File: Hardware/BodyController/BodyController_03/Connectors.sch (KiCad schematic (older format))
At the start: 10 parts, among them J1 7807, J10 7807, J11 7807, J2 CONN_01X08, J3 CONN_01X06, J5 CONN_01X14, J6 CONN_01X02, J7 CONN_01X06, J8 USB_OTG, J9 CONN_01X14

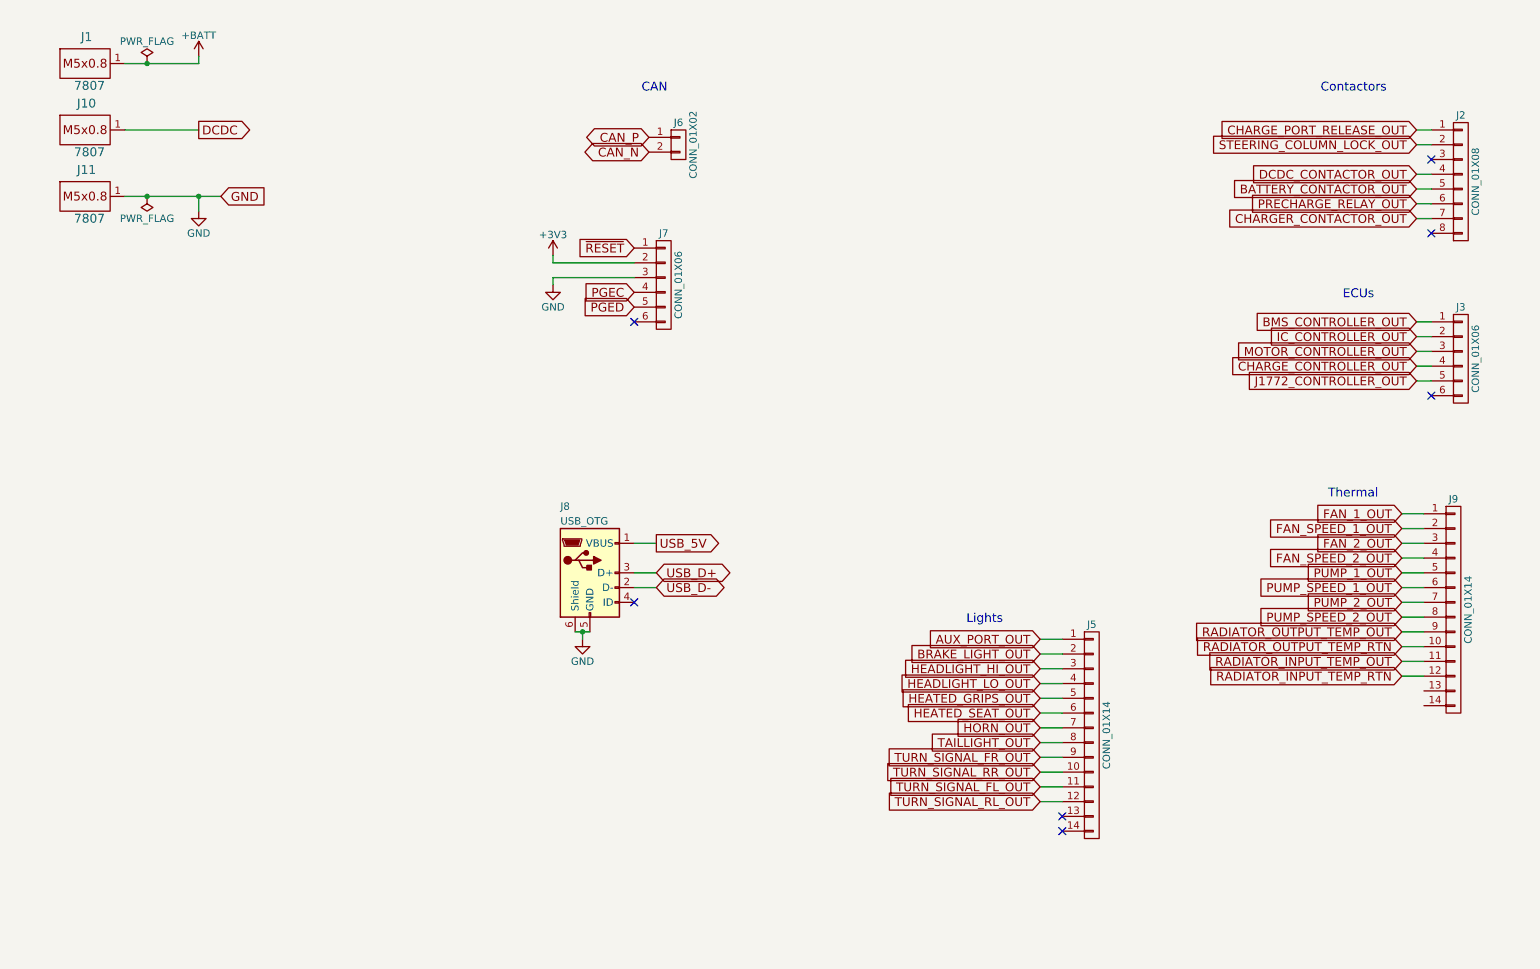
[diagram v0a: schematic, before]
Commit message: Updated layout, cleaned up directory, and modified BOM
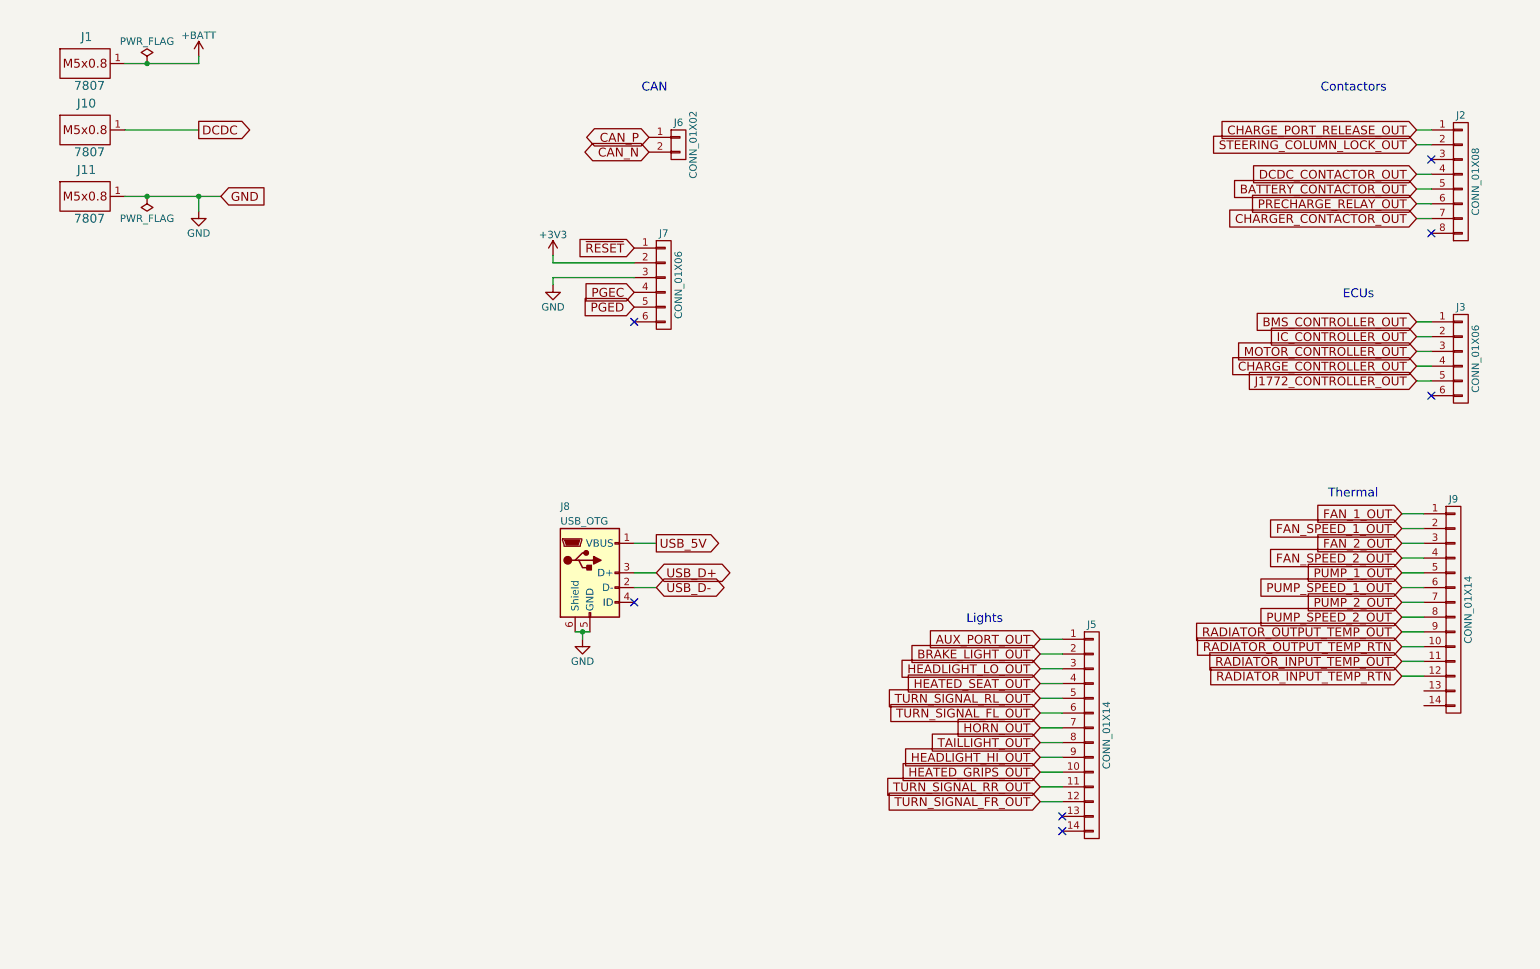
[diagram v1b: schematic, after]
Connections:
- net HEADLIGHT_HI_OUT: now also J5.9 (P9); no longer J5.3 (P3)
- net HEADLIGHT_LO_OUT: now also J5.3 (P3); no longer J5.4 (P4)
- net HEATED_GRIPS_OUT: now also J5.10 (P10); no longer J5.5 (P5)
- net HEATED_SEAT_OUT: now also J5.4 (P4); no longer J5.6 (P6)
- net TURN_SIGNAL_FL_OUT: now also J5.6 (P6); no longer J5.11 (P11)
- net TURN_SIGNAL_FR_OUT: now also J5.12 (P12); no longer J5.9 (P9)
- net TURN_SIGNAL_RL_OUT: now also J5.5 (P5); no longer J5.12 (P12)
- net TURN_SIGNAL_RR_OUT: now also J5.11 (P11); no longer J5.10 (P10)
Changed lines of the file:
@@
 EESchema Schematic File Version 2
+LIBS:BodyController_03-rescue
 LIBS:power
 LIBS:device
@@
 LIBS:contrib
 LIBS:valves
-LIBS:HSD
-LIBS:micros
-LIBS:ICs
-LIBS:Connectors
 LIBS:BodyController_03-cache
 EELAYER 25 0
@@
 Text GLabel 7500 4950 0    59   Input ~ 0
 AUX_PORT_OUT
+Text GLabel 7500 5750 0    59   Input ~ 0
+HEADLIGHT_HI_OUT
 Text GLabel 7500 5150 0    59   Input ~ 0
-HEADLIGHT_HI_OUT
+HEADLIGHT_LO_OUT
+Text GLabel 7500 6050 0    59   Input ~ 0
+TURN_SIGNAL_FR_OUT
+Text GLabel 7500 5950 0    59   Input ~ 0
+TURN_SIGNAL_RR_OUT
+Text GLabel 7500 5450 0    59   Input ~ 0
+TURN_SIGNAL_FL_OUT
+Text GLabel 7500 5350 0    59   Input ~ 0
+TURN_SIGNAL_RL_OUT
+Text GLabel 7500 5850 0    59   Input ~ 0
+HEATED_GRIPS_OUT
 Text GLabel 7500 5250 0    59   Input ~ 0
-HEADLIGHT_LO_OUT
-Text GLabel 7500 5750 0    59   Input ~ 0
-TURN_SIGNAL_FR_OUT
-Text GLabel 7500 5850 0    59   Input ~ 0
-TURN_SIGNAL_RR_OUT
-Text GLabel 7500 5950 0    59   Input ~ 0
-TURN_SIGNAL_FL_OUT
-Text GLabel 7500 6050 0    59   Input ~ 0
-TURN_SIGNAL_RL_OUT
-Text GLabel 7500 5350 0    59   Input ~ 0
-HEATED_GRIPS_OUT
-Text GLabel 7500 5450 0    59   Input ~ 0
 HEATED_SEAT_OUT
 Text GLabel 7500 5650 0    59   Input ~ 0
@@
 	1800 1950 1800 2050
 Wire Wire Line
-	1300 1950 1450 1950
-Wire Wire Line
-	1450 1950 1800 1950
-Wire Wire Line
-	1800 1950 1950 1950
+	1300 1950 1950 1950
 Wire Wire Line
 	1800 1050 1800 1000
 Wire Wire Line
-	1300 1050 1450 1050
-Wire Wire Line
-	1450 1050 1800 1050
+	1300 1050 1800 1050
 Wire Wire Line
 	1800 1500 1300 1500
@@
 	4900 4600 4750 4600
 Wire Wire Line
-	4350 4900 4400 4900
-Wire Wire Line
-	4400 4900 4450 4900
+	4350 4900 4450 4900
 Wire Wire Line
 	4400 4950 4400 4900

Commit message: started serious layout
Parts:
- removed J1, J10, J11: 7807, Footprints:7807, symbol 7807
- removed J2: CONN_01X08, Connectors_Molex:Molex_MegaFit_2x04x5.70mm_Straight, symbol CONN_01X08
- removed J3: CONN_01X06, Connectors_Molex:Molex_MegaFit_2x03x5.70mm_Straight, symbol CONN_01X06
- removed J5, J9: CONN_01X14, Connectors_Molex:Molex_MegaFit_2x06x5.70mm_Straight, symbol CONN_01X14
- removed J6: CONN_01X02, Connectors_Molex:Molex_MegaFit_2x01x5.70mm_Straight, symbol CONN_01X02
- added J1, J5, J6: 7796, Footprints:7796, symbol 7796
- added J2: Conn_01x14, Footprints:34772-0140, symbol Conn_01x14
- added J3, J4: Conn_02x10_Top_Bottom, Footprints:34690-0200, symbol Conn_02x10_Top_Bottom
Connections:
- net +BATT: now also J1.1
- net AUX_PORT_OUT: now also J2.12 (Pin_12)
- net BATTERY_CONTACTOR_OUT: now also J3.11 (Pin_11)
- net BMS_CONTROLLER_OUT: now also J3.6 (Pin_6)
- net BRAKE_LIGHT_OUT: now also J2.1 (Pin_1)
- net CAN_N: now also J4.20 (Pin_20)
- net CAN_P: now also J4.19 (Pin_19)
- net CHARGER_CONTACTOR_OUT: now also J3.9 (Pin_9)
- net CHARGE_CONTROLLER_OUT: now also J3.3 (Pin_3)
- net CHARGE_PORT_RELEASE_OUT: now also J3.8 (Pin_8)
- net DCDC: now also J5.1
- net DCDC_CONTACTOR_OUT: now also J3.12 (Pin_12)
- net FAN_1_OUT: now also J3.2 (Pin_2)
- net GND: now also J6.1
- net HEADLIGHT_HI_OUT: now also J2.4 (Pin_4)
- net HEADLIGHT_LO_OUT: now also J2.3 (Pin_3)
- net HEATED_GRIPS_OUT: now also J2.6 (Pin_6)
- net HEATED_SEAT_OUT: now also J2.5 (Pin_5)
- net HORN_OUT: now also J2.11 (Pin_11)
- net IC_CONTROLLER_OUT: now also J4.1 (Pin_1)
- net J1772_CONTROLLER_OUT: now also J3.5 (Pin_5)
- net MOTOR_CONTROLLER_OUT: now also J3.4 (Pin_4)
- net PRECHARGE_RELAY_OUT: now also J3.10 (Pin_10)
- net PUMP_1_OUT: now also J3.1 (Pin_1)
- net STEERING_COLUMN_LOCK_OUT: now also J3.7 (Pin_7)
- net TAILLIGHT_OUT: now also J2.2 (Pin_2)
- net TURN_SIGNAL_FL_OUT: now also J2.8 (Pin_8)
- net TURN_SIGNAL_FR_OUT: now also J2.10 (Pin_10)
- net TURN_SIGNAL_RL_OUT: now also J2.7 (Pin_7)
- net TURN_SIGNAL_RR_OUT: now also J2.9 (Pin_9)
- new net BRAKE_SWITCH_1: J4.13 (Pin_13)
- new net BRAKE_SWITCH_2: J4.14 (Pin_14)
- new net BRIGHTS_SWITCH: J4.4 (Pin_4)
- new net DAC_OUT_1: J4.15 (Pin_15)
- new net DAC_OUT_2: J4.16 (Pin_16)
- new net HORN_SWITCH: J4.5 (Pin_5)
- new net INGITION_SWITCH: J4.9 (Pin_9)
- new net KICKSTAND_SWITCH: J4.6 (Pin_6)
- new net KILL_SWITCH: J4.10 (Pin_10)
- new net SPARE_SWITCH_1: J4.7 (Pin_7)
- new net SPARE_SWITCH_2: J4.8 (Pin_8)
- new net THROTTLE_SIGNAL: J4.12 (Pin_12)
- new net TURN_LEFT_SWITCH: J4.2 (Pin_2)
- new net TURN_RIGHT_SWITCH: J4.3 (Pin_3)
- no-connect marks 7 -> 9
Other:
- note removed: "CAN"
- note removed: "Contactors"
- note removed: "ECUs"
- note removed: "Lights"
- note removed: "Thermal"
- moved on the sheet: J7, J8

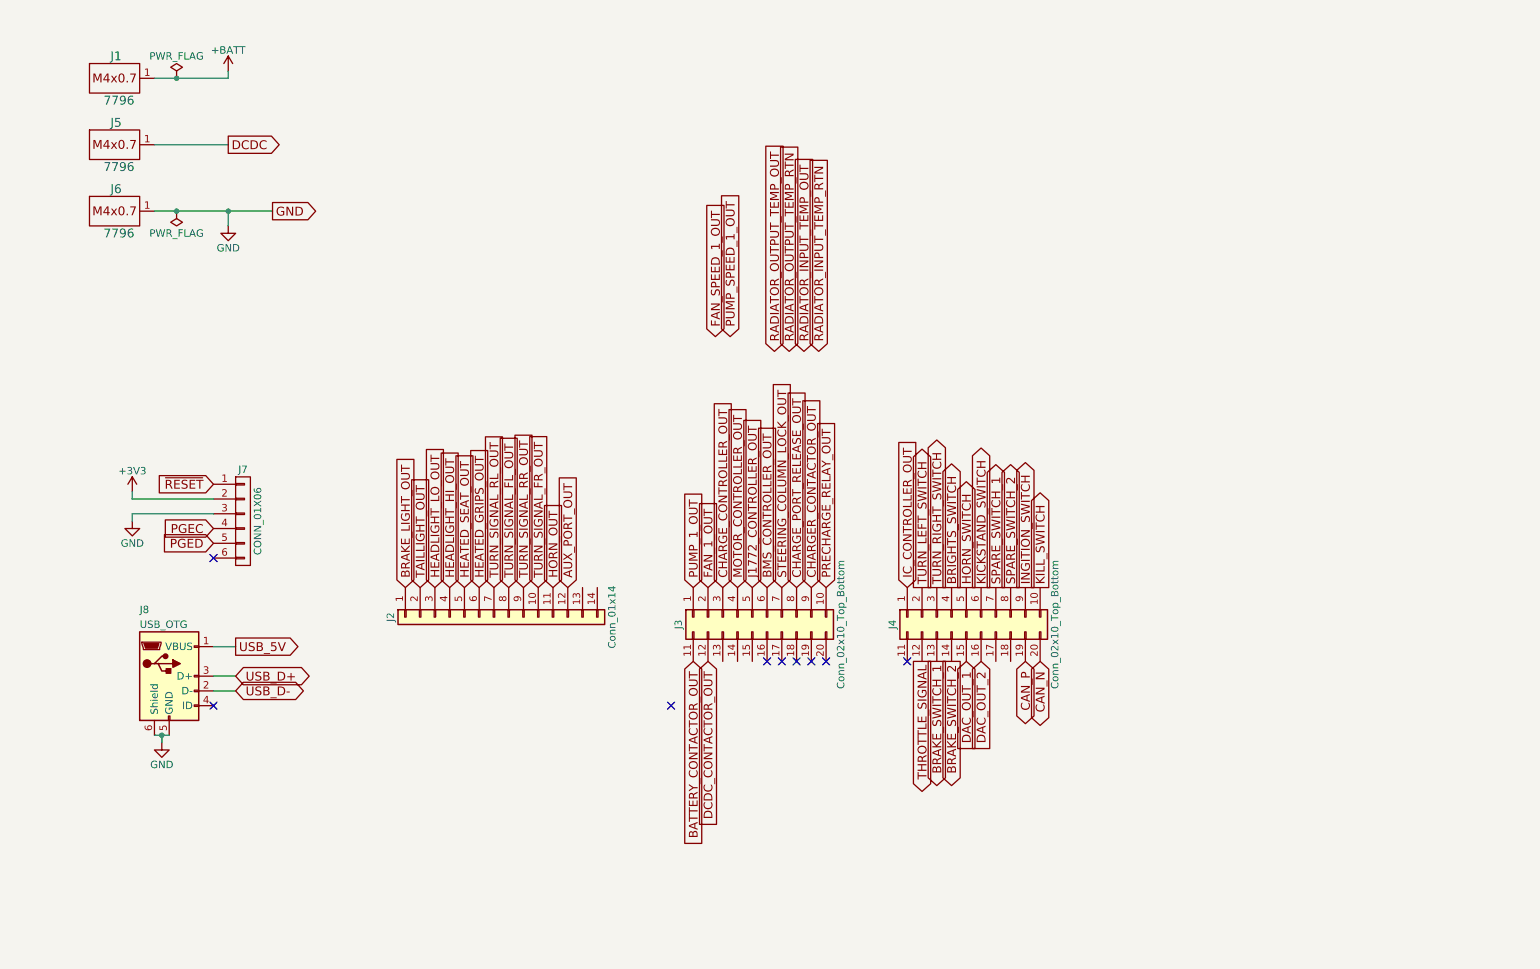
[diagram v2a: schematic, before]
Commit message: Body Controller Layout Done
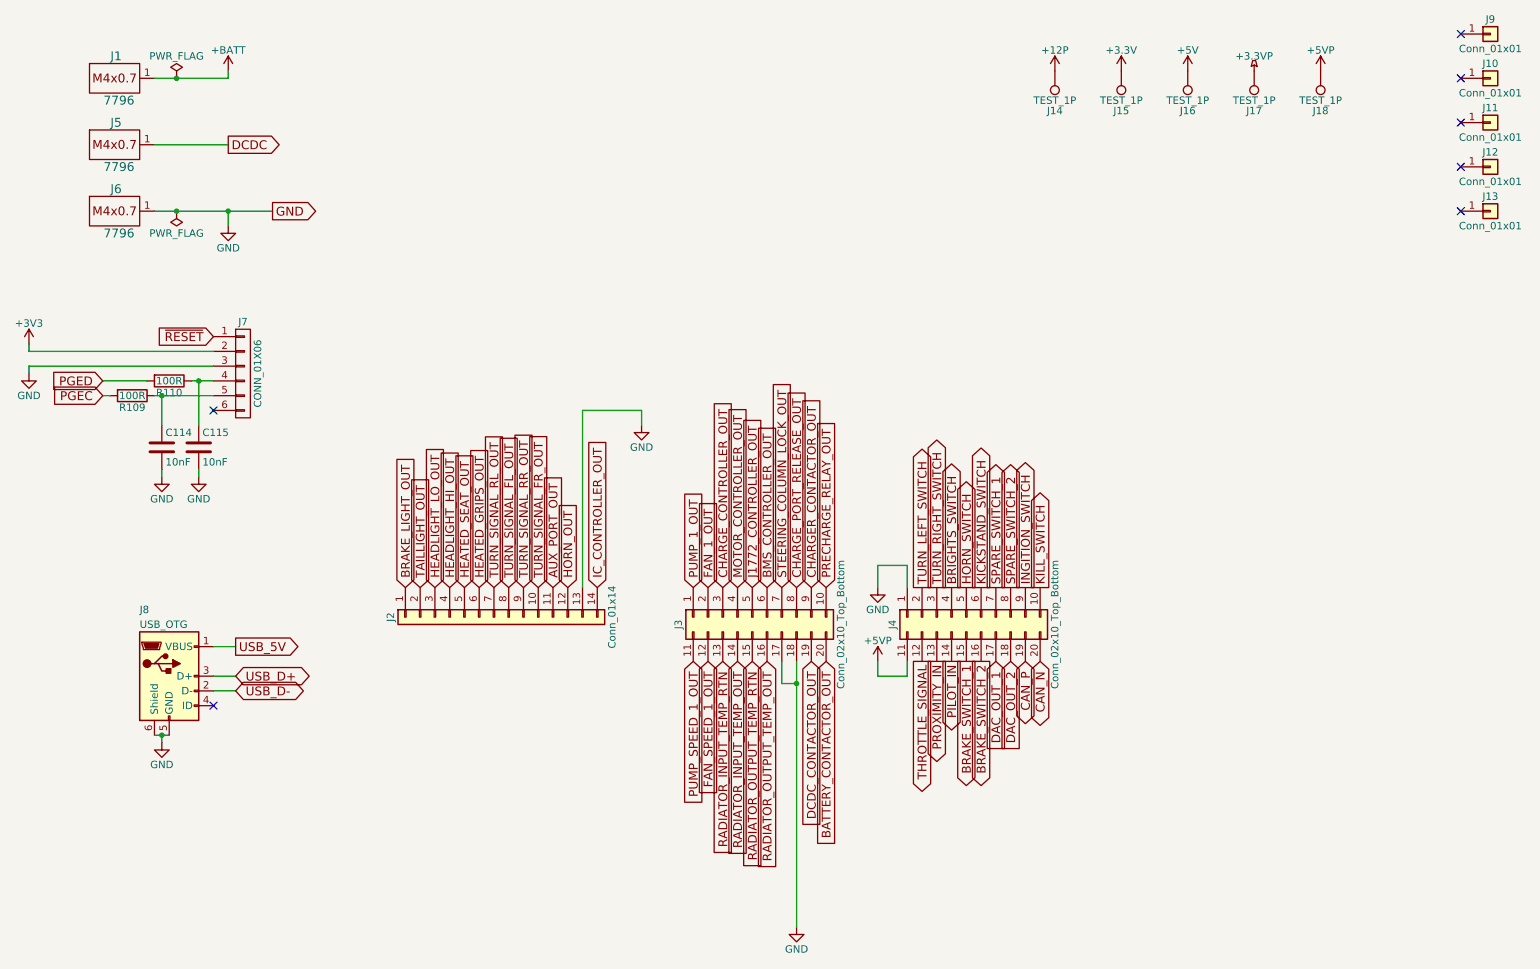
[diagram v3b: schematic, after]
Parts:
- added C114, C115: 10nF, Capacitors_SMD:C_0603, symbol C
- added J10, J11, J12, J13, J9: Conn_01x01, Mounting_Holes:MountingHole_3.2mm_M3_Pad_Via, symbol Conn_01x01
- added J14, J15, J16, J17, J18: TEST_1P, Measurement_Points:Test_Point_Keystone_5019_Minature, symbol TEST_1P
- added R109, R110: 100R, Resistors_SMD:R_0603, symbol R
- J1, J5, J6: PartNumber (none) -> 7796
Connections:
- net +3V3: now also J15.1
- net AUX_PORT_OUT: now also J2.11 (Pin_11); no longer J2.12 (Pin_12)
- net BATTERY_CONTACTOR_OUT: now also J3.20 (Pin_20); no longer J3.11 (Pin_11)
- net BRAKE_SWITCH_1: now also J4.15 (Pin_15); no longer J4.13 (Pin_13)
- net BRAKE_SWITCH_2: now also J4.16 (Pin_16); no longer J4.14 (Pin_14)
- net DAC_OUT_1: now also J4.17 (Pin_17); no longer J4.15 (Pin_15)
- net DAC_OUT_2: now also J4.18 (Pin_18); no longer J4.16 (Pin_16)
- net DCDC_CONTACTOR_OUT: now also J3.19 (Pin_19); no longer J3.12 (Pin_12)
- net FAN_SPEED_1_OUT: now also J3.12 (Pin_12)
- net GND: now also J2.13 (Pin_13), J3.17 (Pin_17), J3.18 (Pin_18), J4.1 (Pin_1), C114.2, C115.2
- net HORN_OUT: now also J2.12 (Pin_12); no longer J2.11 (Pin_11)
- net IC_CONTROLLER_OUT: now also J2.14 (Pin_14); no longer J4.1 (Pin_1)
- net PGEC: now also R109.2; no longer J7.4 (P4)
- net PGED: now also R110.2; no longer J7.5 (P5)
- net PUMP_SPEED_1_OUT: now also J3.11 (Pin_11)
- net RADIATOR_INPUT_TEMP_OUT: now also J3.14 (Pin_14)
- net RADIATOR_INPUT_TEMP_RTN: now also J3.13 (Pin_13)
- net RADIATOR_OUTPUT_TEMP_OUT: now also J3.16 (Pin_16)
- net RADIATOR_OUTPUT_TEMP_RTN: now also J3.15 (Pin_15)
- net +5VP: now reaches J4.11 (Pin_11)
- net +5VP: now also J18.1
- new net: C115.1, J7.4 (P4), R110.1
- new net: C114.1, J7.5 (P5), R109.1
- new net +12P: J14.1
- new net +3.3VP: J17.1
- new net +5V: J16.1
- new net PILOT_IN: J4.14 (Pin_14)
- new net PROXIMITY_IN: J4.13 (Pin_13)
- no-connect marks 9 -> 7
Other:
- moved on the sheet: J7
